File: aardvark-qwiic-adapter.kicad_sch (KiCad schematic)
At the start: 7 parts, among them J1 Conn_02x05_Odd_Even, J2 Conn_01x04, J3 Conn_01x04, J4 Conn_01x02, U1 AP7361C-33E

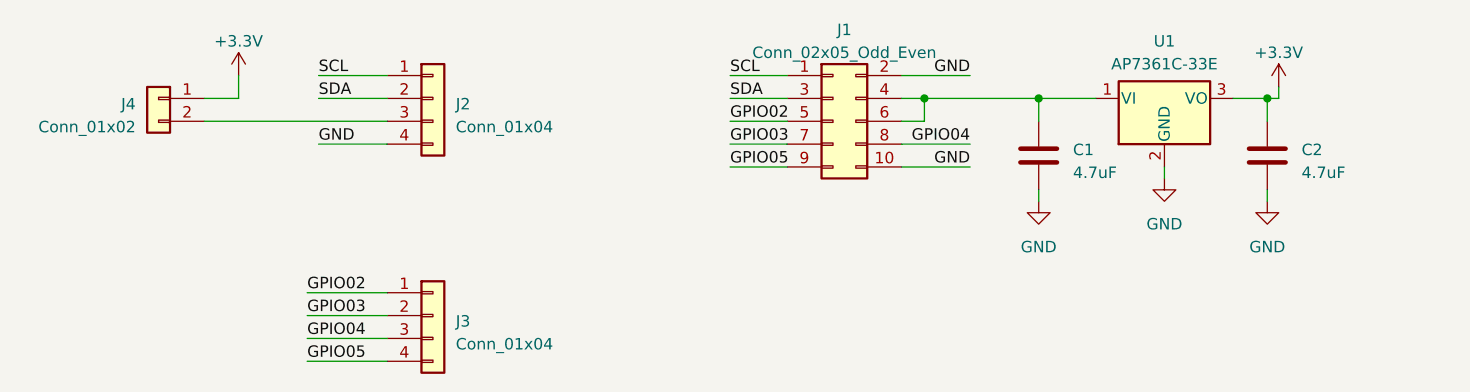
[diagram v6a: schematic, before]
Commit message: Place components, 3d models
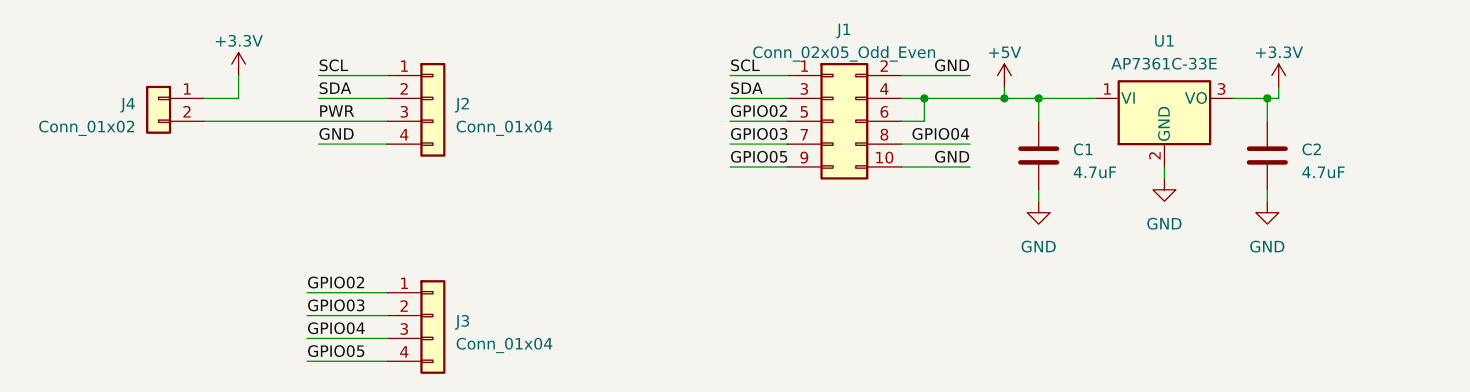
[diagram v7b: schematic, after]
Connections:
- net +5V: now reaches C1.1, J1.4 (Pin_4), J1.6 (Pin_6), U1.1 (VI)
- net PWR: now reaches J2.3 (Pin_3), J4.2 (Pin_2)
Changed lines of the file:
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@@
   (junction (at 151.13 93.98) (diameter 0) (color 0 0 0 0)
   )
+  (junction (at 160.02 93.98) (diameter 0) (color 0 0 0 0)
+  )
   (junction (at 189.23 93.98) (diameter 0) (color 0 0 0 0)
   )
@@
     (stroke (width 0) (type default))
   )
-  (wire (pts (xy 151.13 93.98) (xy 163.83 93.98))
+  (wire (pts (xy 151.13 93.98) (xy 160.02 93.98))
     (stroke (width 0) (type default))
   )
@@
     (stroke (width 0) (type default))
   )
+  (wire (pts (xy 160.02 92.71) (xy 160.02 93.98))
+    (stroke (width 0) (type default))
+  )
   (wire (pts (xy 148.59 91.44) (xy 156.21 91.44))
     (stroke (width 0) (type default))
@@
   )
   (wire (pts (xy 189.23 104.14) (xy 189.23 105.41))
+    (stroke (width 0) (type default))
+  )
+  (wire (pts (xy 160.02 93.98) (xy 163.83 93.98))
     (stroke (width 0) (type default))
   )
@@
   )
   (label "GPIO03" (at 82.55 118.11 0) (fields_autoplaced)
+    (effects (font (size 1.27 1.27)) (justify left bottom))
+  )
+  (label "PWR" (at 83.82 96.52 0) (fields_autoplaced)
     (effects (font (size 1.27 1.27)) (justify left bottom))
   )
@@
         )
       )
+    )
+  )
+  (symbol (lib_id "power:+5V") (at 160.02 92.71 0) (unit 1)
+    (in_bom yes) (on_board yes) (dnp no) (fields_autoplaced)
+    (property "Reference" "#PWR06" (at 160.02 96.52 0)
+      (effects (font (size 1.27 1.27)) hide)
+    )
+    (property "Value" "+5V" (at 160.02 88.9 0)
+      (effects (font (size 1.27 1.27)))
+    )
+    (property "Footprint" "" (at 160.02 92.71 0)
+      (effects (font (size 1.27 1.27)) hide)
+    )
+    (property "Datasheet" "" (at 160.02 92.71 0)
+      (effects (font (size 1.27 1.27)) hide)
+    )
+    (pin "1")
+    (instances
+      (project "aardvark-qwiic-adapter"
+        (path "/dd35b9f1-2797-46a7-a3ff-4e2c1be5fc91"
+          (reference "#PWR06") (unit 1)
+        )
+      )

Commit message: ERC
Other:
- moved on the sheet: C1, C2, U1
